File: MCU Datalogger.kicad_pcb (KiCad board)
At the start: 2 copper layers, 56.9 x 36.6 mm, 30 parts, among them J1 Conn_01x09_Pin, J2 Conn_01x04_Pin, J3 Conn_01x04_Pin, J4 Conn_02x03_Odd_Even, U1 DS1337S_, U2 24LC1025, U3 24LC1025, U4 ATMEGA328P-AU, Y1 32.768 KHz, Y2 16 MHz

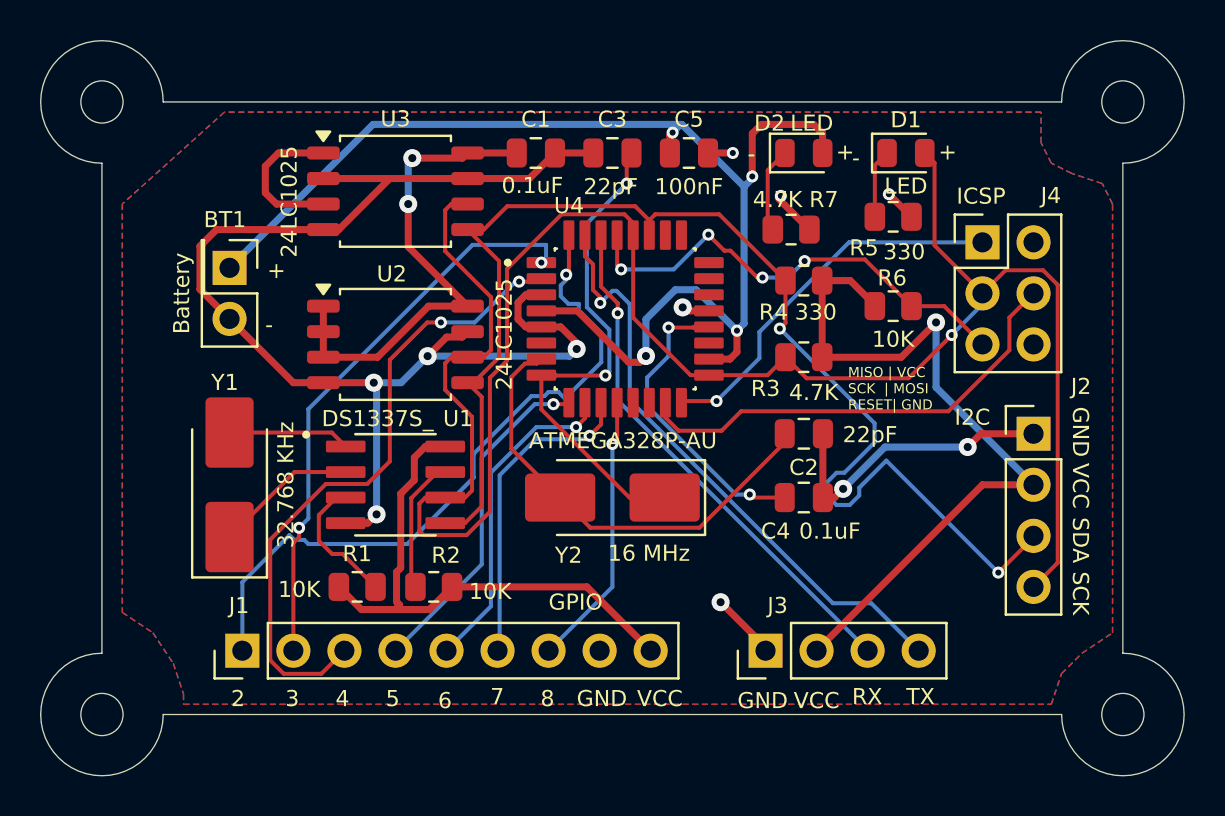
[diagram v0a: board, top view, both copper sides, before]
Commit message: update SCL route on pcb
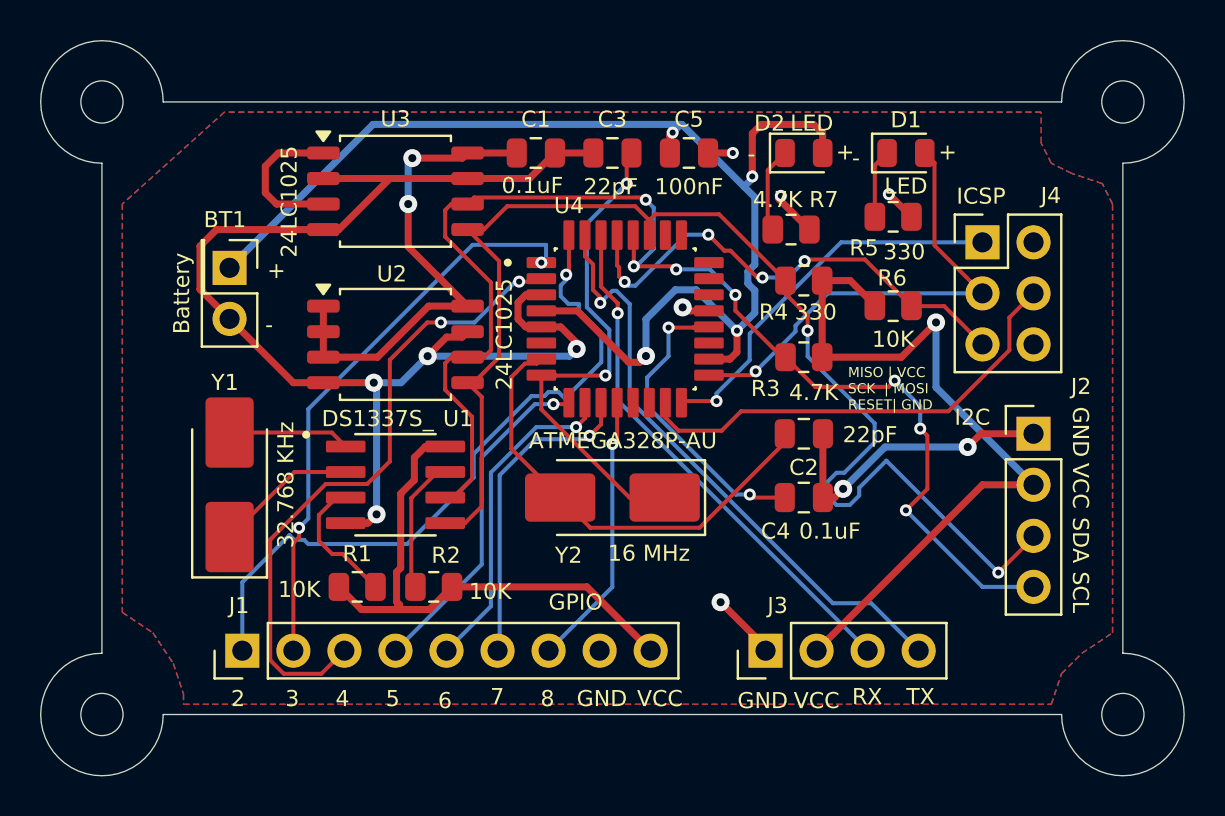
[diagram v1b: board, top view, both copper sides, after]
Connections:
- net Net-(U4-AREF) renamed /Abc123
- J2 pad 4: /SCK -> /SCL
- R3 pad 2: /SCK -> /SCL
- U1 pad 6: /SCK -> /SCL
- U2 pad 6: /SCK -> /SCL
- U3 pad 6: /SCK -> /SCL
- U4 pad 28: /SCK -> /SCL
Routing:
- net /SCK: track 101.3 -> 24.2 mm
- net /SCL: track 0.00 -> 65.8 mm, vias 0 -> 7
- net /RESET: track 23.5 -> 24.4 mm
- net /VCC: track 160.9 -> 161.6 mm
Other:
- board text added: "SCL"
- board text removed: "SCK"
